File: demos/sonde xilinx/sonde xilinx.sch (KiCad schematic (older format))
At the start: 25 parts, among them J1 DB25MALE, J2 DB9MALE, P1 CONN_6, U1 74LS125, U2 74LS125

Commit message: Some demo files updated.
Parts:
- removed C4: 100pF, symbol C
- added C5: 100pF, symbol C
- renumbered C5 to C4
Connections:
- net GND: now also C5.2
- net at R12.2, U1.8 (O): now also C5.1; no longer C4.1
- net at R13.2, U1.11 (O): now also C4.1
- net CLK(D1) renamed CLK-D1
- net CTRL(D3) renamed CTRL-D3
- net DONE(/SELECT) renamed DONE-SELECT*
- net PWR(3,3-5V) renamed PWR_3,3-5V
- net TD0-DONE/P renamed TD0-DONE
- net TD0/PROG(D4) renamed TD0-PROG-D4
- net TDI/DIN(D0) renamed TDI-DIN-D0
- net TMS/PROG(D2) renamed TMS-PROG-D2
- net VCC_SENSE(/ERROR) renamed VCC_SENSE-ERROR*
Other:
- moved on the sheet: C4
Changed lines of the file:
@@
-EESchema Schematic File Version 2  date 09/02/2011 18:36:39
+EESchema Schematic File Version 2  date 10/02/2011 12:23:20
 LIBS:power
 LIBS:device
@@
 Sheet 1 1
 Title "CABLE PARALLELE III"
-Date "9 feb 2011"
+Date "10 feb 2011"
 Rev "1"
 Comp ""
@@
 Comment4 ""
 $EndDescr
+$Comp
+L R R11
+U 1 1 4D527316
+P 6650 2600
+F 0 "R11" V 6730 2600 50  0000 C CNN
+F 1 "100" V 6650 2600 50  0000 C CNN
+	1    6650 2600
+	0    1    1    0
+$EndComp
 Wire Wire Line
 	6900 4200 7350 4200
@@
 	6400 4200 5900 4200
 $Comp
-L GND #PWR111
-U 1 1 4D52D0AC
+L GND #PWR01
+U 1 1 3EBF81B1
 P 6300 4650
-F 0 "#PWR111" H 6300 4650 40  0001 C CNN
+F 0 "#PWR01" H 6300 4650 40  0001 C CNN
 F 1 "GND" H 6300 4580 40  0001 C CNN
 	1    6300 4650
@@
 $Comp
 L C C4
-U 1 1 4D52D0AA
+U 1 1 3EBF81A7
 P 6300 4450
 F 0 "C4" H 6350 4550 50  0000 L CNN
@@
 $Comp
 L R R13
-U 1 1 4D52D0A6
+U 1 1 4D528082
 P 6650 4200
 F 0 "R13" V 6730 4200 50  0000 C CNN
@@
 	8400 3700 8400 2750
 $Comp
-L PWR_FLAG #FLG102
+L PWR_FLAG #FLG02
 U 1 1 3EBF848F
 P 6200 1050
-F 0 "#FLG102" H 6200 1320 30  0001 C CNN
+F 0 "#FLG02" H 6200 1320 30  0001 C CNN
 F 1 "PWR_FLAG" H 6200 1280 30  0000 C CNN
 	1    6200 1050
@@
 $EndComp
 $Comp
-L VCC #PWR106
+L VCC #PWR03
 U 1 1 3EBF8479
 P 5900 1050
-F 0 "#PWR106" H 5900 1150 30  0001 C CNN
+F 0 "#PWR03" H 5900 1150 30  0001 C CNN
 F 1 "VCC" H 5900 1150 30  0000 C CNN
 	1    5900 1050
@@
 $EndComp
 $Comp
-L GND #PWR101
+L GND #PWR04
 U 1 1 3EBF8458
 P 800 7300
-F 0 "#PWR101" H 800 7300 40  0001 C CNN
+F 0 "#PWR04" H 800 7300 40  0001 C CNN
 F 1 "GND" H 800 7230 40  0001 C CNN
 	1    800  7300
@@
 $EndComp
 $Comp
-L PWR_FLAG #FLG101
+L PWR_FLAG #FLG05
 U 1 1 3EBF843C
 P 800 7300
-F 0 "#FLG101" H 800 7570 30  0001 C CNN
+F 0 "#FLG05" H 800 7570 30  0001 C CNN
 F 1 "PWR_FLAG" H 800 7530 30  0000 C CNN
 	1    800  7300
@@
 	2500 2700 2200 2700
 $Comp
-L GND #PWR104
-U 1 1 4D52D0A5
+L GND #PWR06
+U 1 1 4D528081
 P 2500 2750
-F 0 "#PWR104" H 2500 2750 40  0001 C CNN
+F 0 "#PWR06" H 2500 2750 40  0001 C CNN
 F 1 "GND" H 2500 2680 40  0001 C CNN
 	1    2500 2750
@@
 	10250 3500 9400 3500
 Text Label 9450 3500 0    60   ~ 0
-PWR(3,3-5V)
-$Comp
-L GND #PWR114
-U 1 1 3EBF8376
+PWR_3,3-5V
+$Comp
+L GND #PWR07
+U 1 1 4D52808A
 P 10050 3600
-F 0 "#PWR114" H 10050 3600 40  0001 C CNN
+F 0 "#PWR07" H 10050 3600 40  0001 C CNN
 F 1 "GND" H 10050 3530 40  0001 C CNN
 	1    10050 3600
@@
 TDI-DIN
 Text Label 7550 2750 0    60   ~ 0
-TD0-DONE/P
+TD0-DONE
 Text Label 7700 2550 0    60   ~ 0
-PWR(3,3-5V)
-$Comp
-L GND #PWR113
-U 1 1 4D52D0AF
+PWR_3,3-5V
+$Comp
+L GND #PWR08
+U 1 1 3EBF8376
 P 8500 2650
-F 0 "#PWR113" H 8500 2650 40  0001 C CNN
+F 0 "#PWR08" H 8500 2650 40  0001 C CNN
 F 1 "GND" H 8500 2580 40  0001 C CNN
 	1    8500 2650
@@
 	6500 1100 6500 1050
 $Comp
-L GND #PWR112
+L GND #PWR09
 U 1 1 3EBF82CF
 P 6500 1500
-F 0 "#PWR112" H 6500 1500 40  0001 C CNN
+F 0 "#PWR09" H 6500 1500 40  0001 C CNN
 F 1 "GND" H 6500 1430 40  0001 C CNN
 	1    6500 1500
@@
 	6400 1900 5900 1900
 $Comp
-L GND #PWR110
-U 1 1 4D52D0AD
+L GND #PWR010
+U 1 1 4D528089
 P 6300 3750
-F 0 "#PWR110" H 6300 3750 40  0001 C CNN
+F 0 "#PWR010" H 6300 3750 40  0001 C CNN
 F 1 "GND" H 6300 3680 40  0001 C CNN
 	1    6300 3750
@@
 $Comp
 L C C5
-U 1 1 3EBF81A7
+U 1 1 4D528086
 P 6300 3550
 F 0 "C5" H 6350 3650 50  0000 L CNN
@@
 $Comp
 L R R12
-U 1 1 4D52D0A7
+U 1 1 4D528083
 P 6650 3300
 F 0 "R12" V 6730 3300 50  0000 C CNN
@@
 $EndComp
 $Comp
-L GND #PWR109
-U 1 1 4D52D0AE
+L GND #PWR011
+U 1 1 4D528088
 P 6300 3050
-F 0 "#PWR109" H 6300 3050 40  0001 C CNN
+F 0 "#PWR011" H 6300 3050 40  0001 C CNN
 F 1 "GND" H 6300 2980 40  0001 C CNN
 	1    6300 3050
@@
 $Comp
 L C C2
-U 1 1 4D52D0AB
+U 1 1 4D528085
 P 6300 2850
 F 0 "C2" H 6350 2950 50  0000 L CNN
@@
 	1    0    0    -1
 $EndComp
-$Comp
-L R R11
-U 1 1 4D52D0A8
-P 6650 2600
-F 0 "R11" V 6730 2600 50  0000 C CNN
-F 1 "100" V 6650 2600 50  0000 C CNN
-	1    6650 2600
-	0    1    1    0
-$EndComp
 Connection ~ 5900 1050
 Connection ~ 6200 1050
@@
 	6200 1050 6200 1100
 $Comp
-L GND #PWR107
+L GND #PWR012
 U 1 1 3EBF81B3
 P 6200 1600
-F 0 "#PWR107" H 6200 1600 40  0001 C CNN
+F 0 "#PWR012" H 6200 1600 40  0001 C CNN
 F 1 "GND" H 6200 1530 40  0001 C CNN
 	1    6200 1600
@@
 $EndComp
 $Comp
-L GND #PWR108
-U 1 1 3EBF81B1
+L GND #PWR013
+U 1 1 4D528087
 P 6300 2350
-F 0 "#PWR108" H 6300 2350 40  0001 C CNN
+F 0 "#PWR013" H 6300 2350 40  0001 C CNN
 F 1 "GND" H 6300 2280 40  0001 C CNN
 	1    6300 2350
@@
 $Comp
 L C C3
-U 1 1 4D52D0A9
+U 1 1 4D528084
 P 6300 2150
 F 0 "C3" H 6350 2250 50  0000 L CNN
@@
 	2500 1700 2200 1700
 $Comp
-L GND #PWR103
+L GND #PWR014
 U 1 1 3EBF8100
 P 2500 1750
-F 0 "#PWR103" H 2500 1750 40  0001 C CNN
+F 0 "#PWR014" H 2500 1750 40  0001 C CNN
 F 1 "GND" H 2500 1680 40  0001 C CNN
 	1    2500 1750
@@
 $EndComp
 $Comp
-L GND #PWR105
+L GND #PWR015
 U 1 1 3EBF80DD
 P 4650 2000
-F 0 "#PWR105" H 4650 2000 40  0001 C CNN
+F 0 "#PWR015" H 4650 2000 40  0001 C CNN
 F 1 "GND" H 4650 1930 40  0001 C CNN
 	1    4650 2000
@@
 Connection ~ 4800 2900
 Text Label 2500 1050 0    60   ~ 0
-VCC_SENSE(/ERROR)
+VCC_SENSE-ERROR*
 Text Label 2400 3800 0    60   ~ 0
-TDI/DIN(D0)
+TDI-DIN-D0
 Text Label 2400 3600 0    60   ~ 0
-CLK(D1)
+CLK-D1
 Text Label 2400 3400 0    60   ~ 0
-TMS/PROG(D2)
+TMS-PROG-D2
 Text Label 2400 3200 0    60   ~ 0
-CTRL(D3)
+CTRL-D3
 Text Label 2400 3000 0    60   ~ 0
-TD0/PROG(D4)
+TD0-PROG-D4
 Wire Wire Line
 	2300 1050 3700 1050
@@
 	3350 2250 3700 2250
 Text Label 2500 1600 0    60   ~ 0
-DONE(/SELECT)
+DONE-SELECT*
 NoConn ~ 2150 6900
 NoConn ~ 2150 6250
@@
 	1700 7200 1150 7200
 $Comp
-L GND #PWR102
+L GND #PWR016
 U 1 1 3EBF7F0D
 P 1150 7300
-F 0 "#PWR102" H 1150 7300 40  0001 C CNN
+F 0 "#PWR016" H 1150 7300 40  0001 C CNN
 F 1 "GND" H 1150 7230 40  0001 C CNN
 	1    1150 7300
@@
 $Comp
 L R R8
-U 1 1 4D52D0A4
+U 1 1 4D528080
 P 3950 2900
 F 0 "R8" V 4030 2900 50  0000 C CNN
@@
 $Comp
 L R R7
-U 1 1 4D52D0A3
+U 1 1 4D52807F
 P 3950 2600
 F 0 "R7" V 4030 2600 50  0000 C CNN

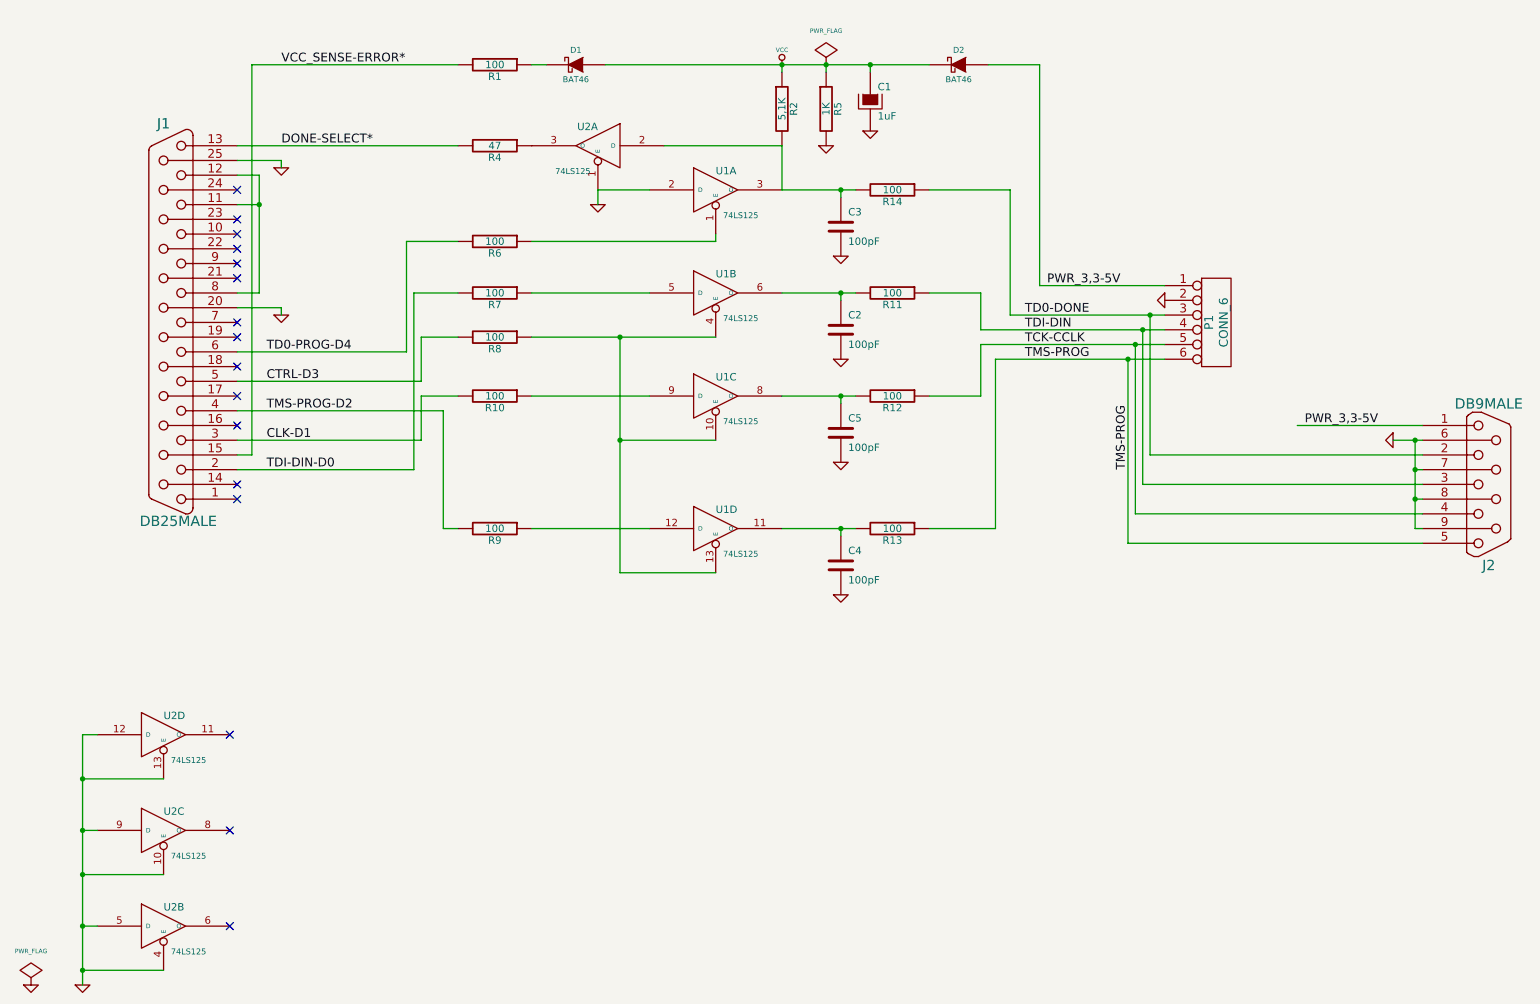
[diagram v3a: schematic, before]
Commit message: demos/ schematic tidying
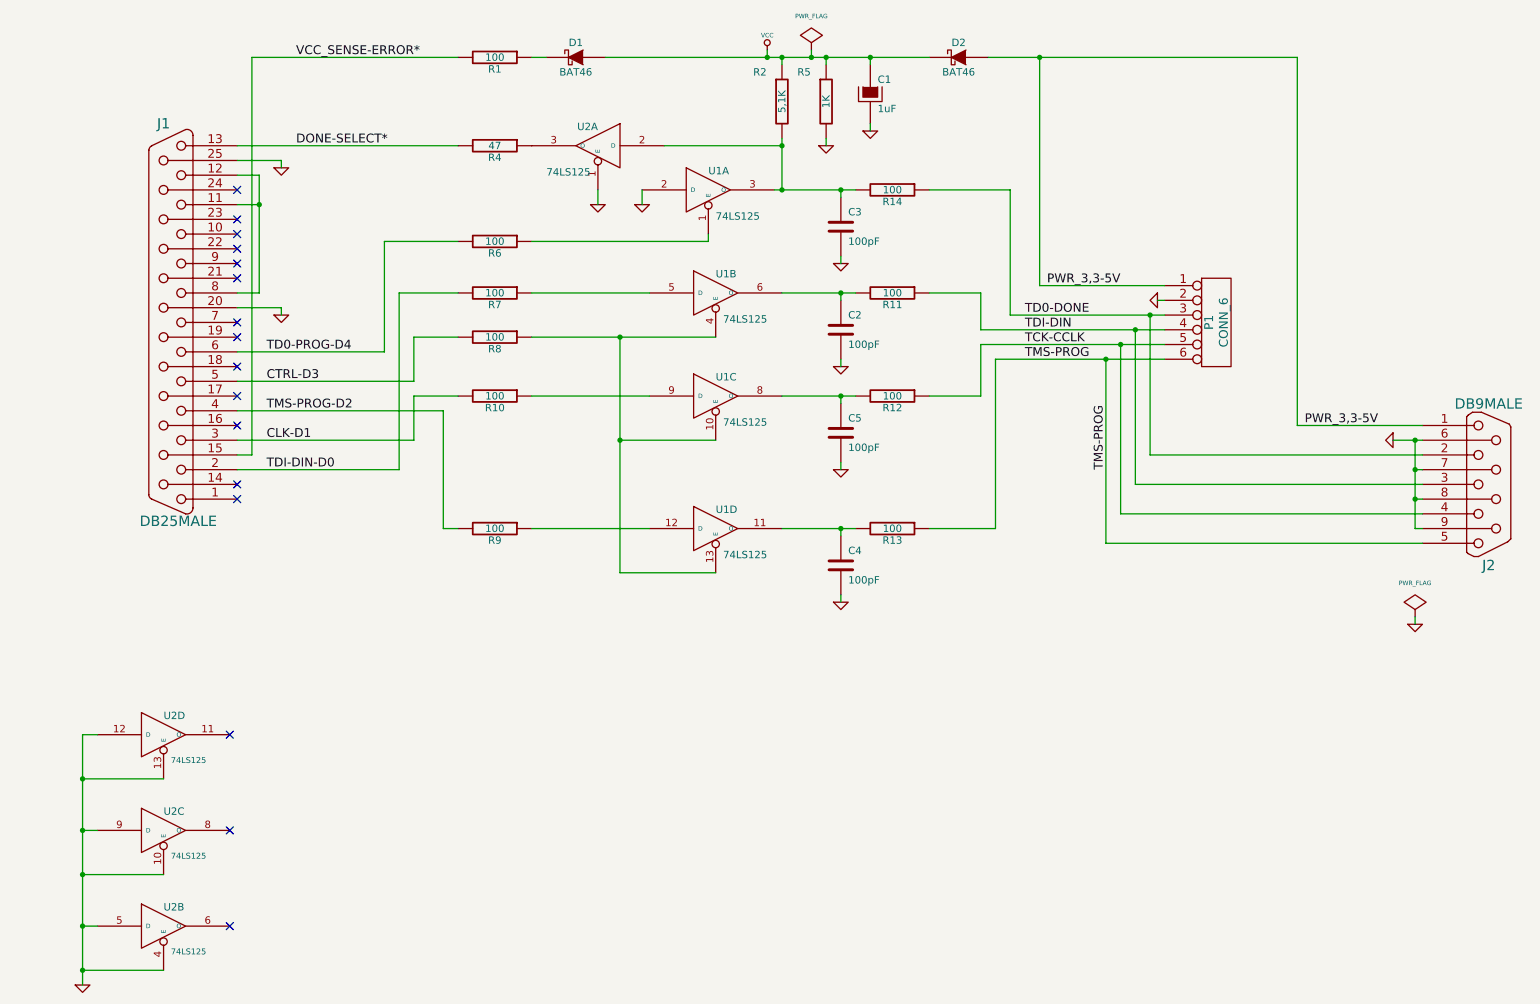
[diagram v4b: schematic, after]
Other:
- moved on the sheet: C1, D1, D2, R1, R2, R5, U1A

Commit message: polygons in footprint body: fix incorrect calculation of polygons with clearance or outline thickness (fix bug #1511366) Clean demos
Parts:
- C1: footprint (none) -> Discret:CP5
- C2, C3, C4, C5: footprint (none) -> Discret:C2
- D1, D2: footprint (none) -> Discret:D3
- J1: footprint (none) -> Connect:DB25M_CI
- J2: footprint (none) -> Connect:DB9M_CI_INVERT
- P1: footprint (none) -> Connect:bornier6
- R1, R10, R11, R12, R13, R14, R2, R4, R5, R6, R7, R8, R9: footprint (none) -> Discret:R4
- U1, U2: footprint (none) -> Sockets_DIP:DIP-14__300_ELL
